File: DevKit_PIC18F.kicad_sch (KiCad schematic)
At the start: 31 parts, among them J1 PIC_ICSP_ICD, J2 USB_C_Receptacle_USB2.0_16P, J3 5P_UART, J4 RA_PORT, J5 RB_PORT, J6 RD_PORT, J7 RC_PORT, J8 RE_PORT, SW1 SW_DIP, X1 16MHz

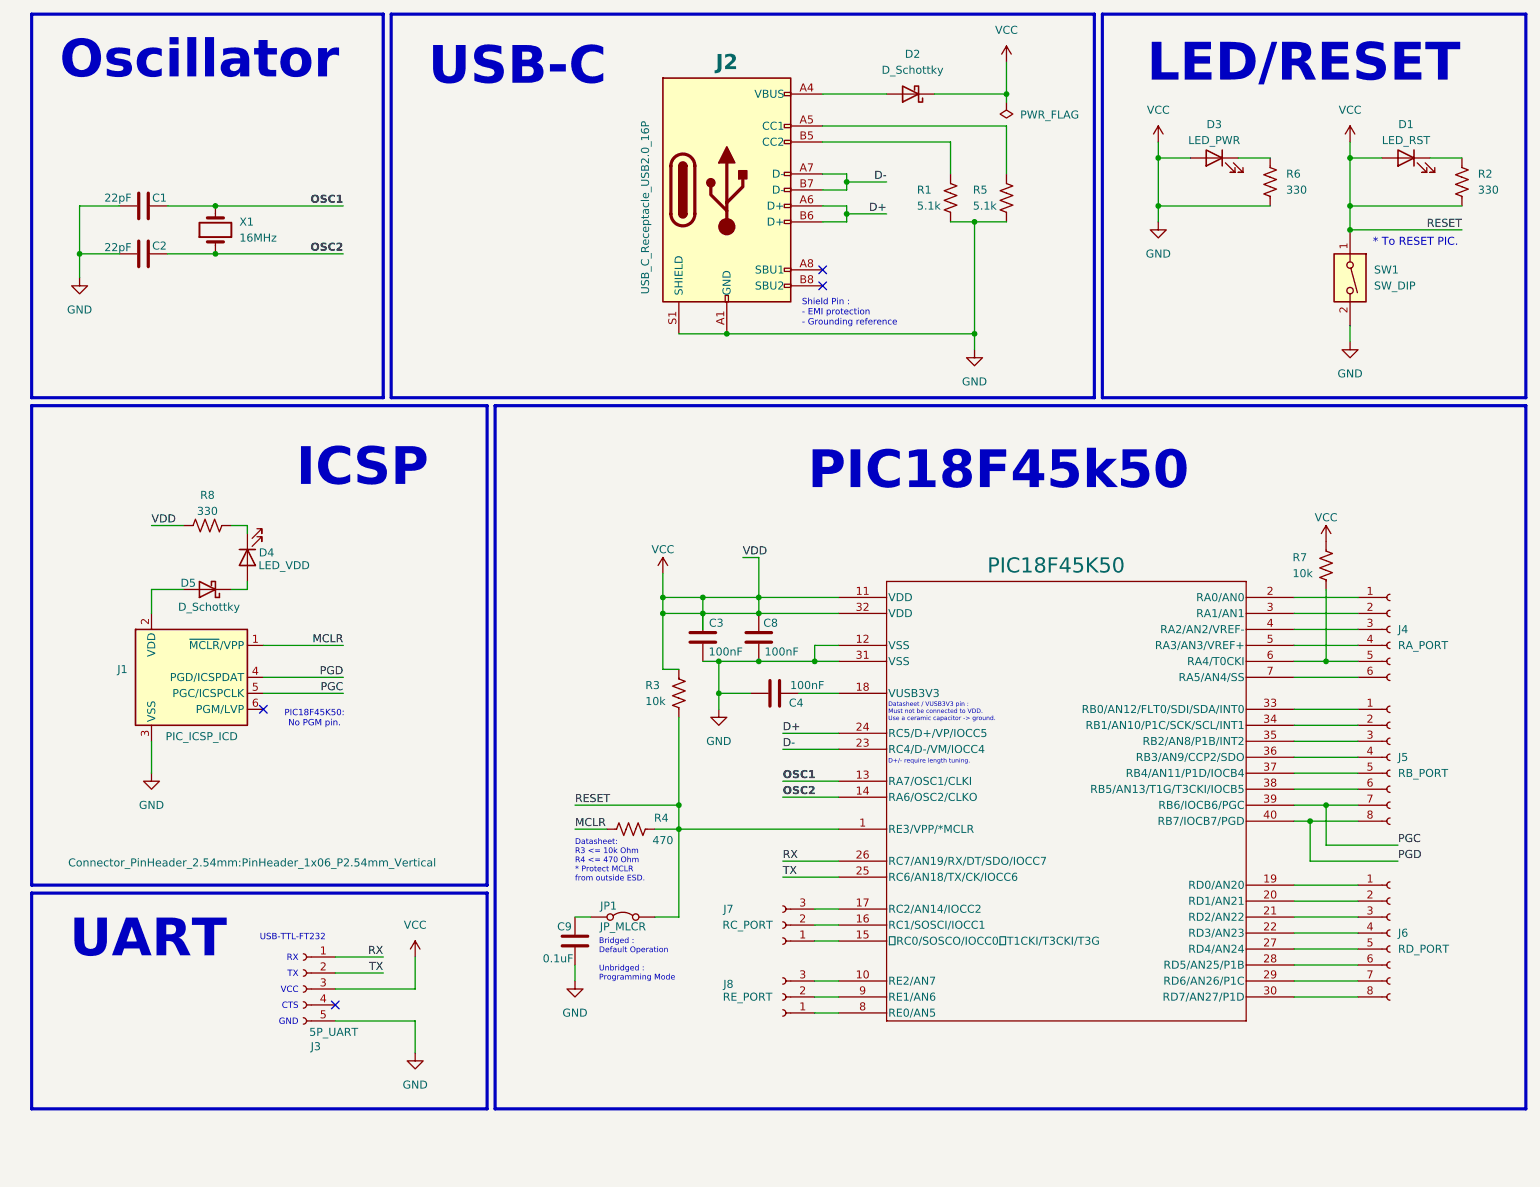
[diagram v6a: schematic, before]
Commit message: refined & ordered to fabricate test pcs.
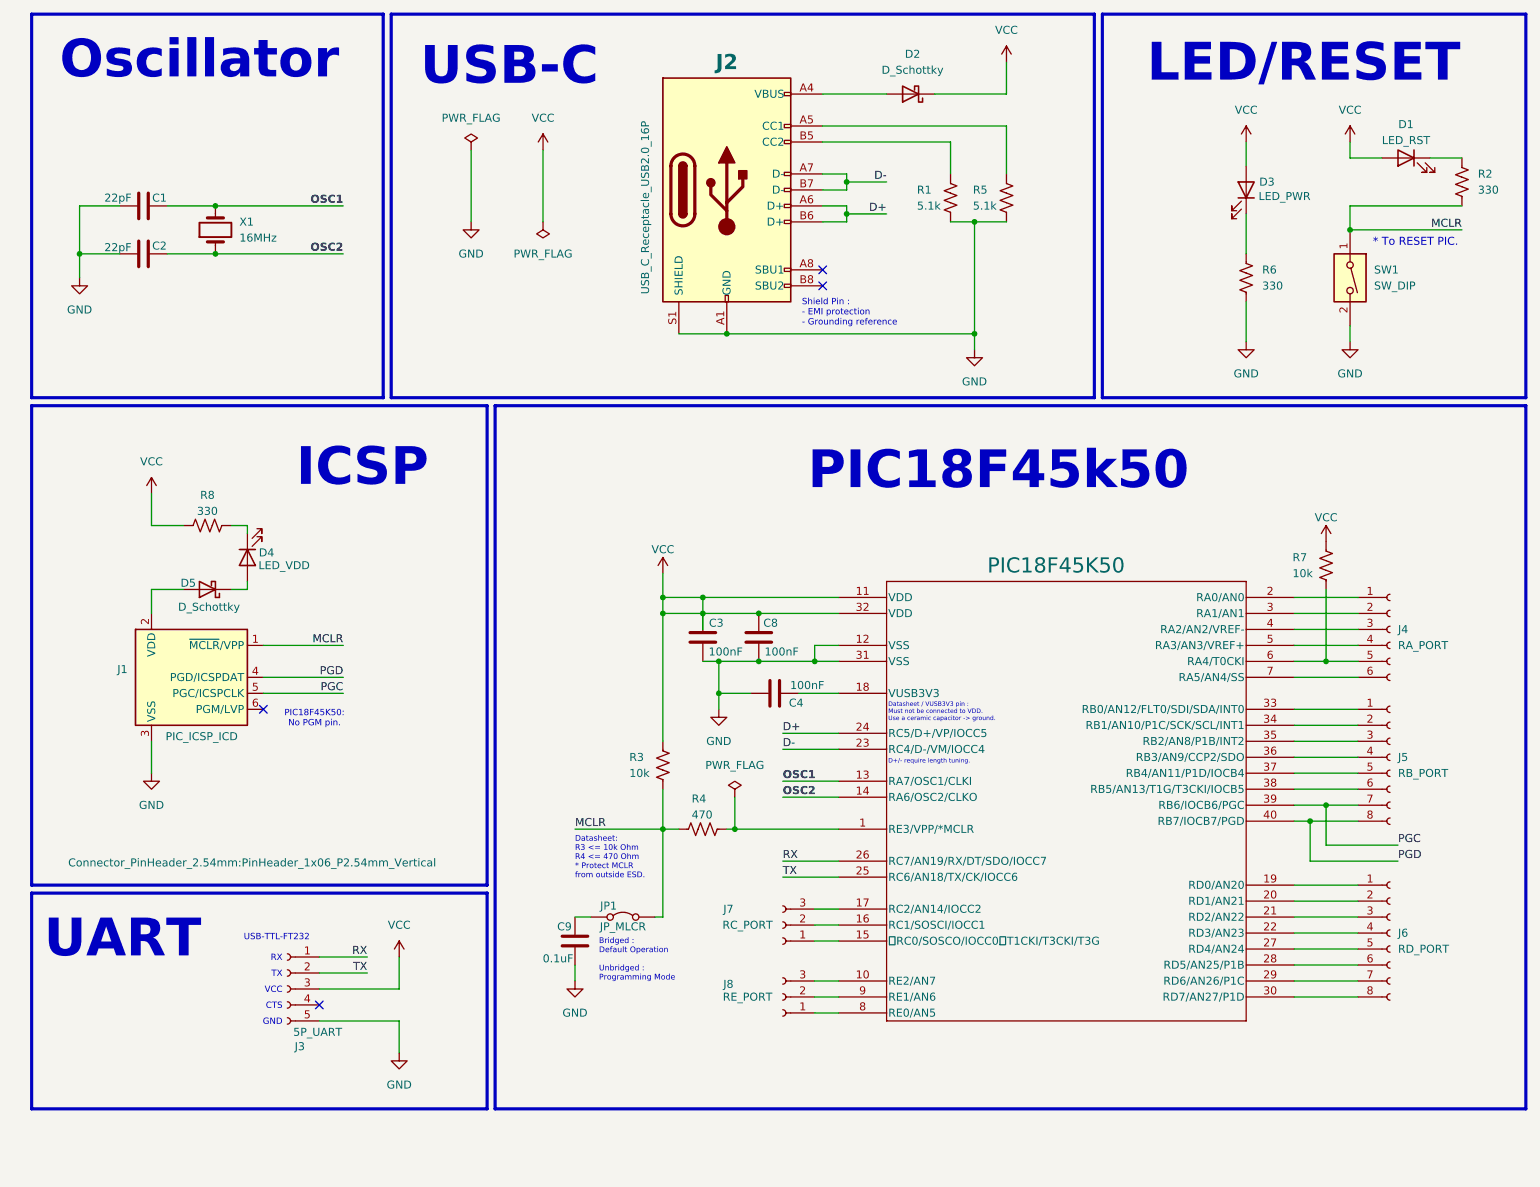
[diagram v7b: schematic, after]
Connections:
- net GND: no longer C3.1, C8.1, D1.2 (A), D2.1 (K), D3.2 (A), J3.3 (Pin_3), JP1.2 (B), PIC18F45K50.1 (RE3/VPP/*MCLR), PIC18F45K50.11 (VDD), PIC18F45K50.32 (VDD), R2.2, R3.1, R3.2, R4.2, R7.1, R8.1, SW1.1
- net MCLR: now also JP1.2 (B), R2.2, R3.2, R4.2, SW1.1; no longer R4.1
- new net: PIC18F45K50.1 (RE3/VPP/*MCLR), R4.1
- new net VCC: C3.1, C8.1, D1.2 (A), D2.1 (K), D3.2 (A), J3.3 (Pin_3), PIC18F45K50.11 (VDD), PIC18F45K50.32 (VDD), R3.1, R7.1, R8.1
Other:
- moved on the sheet: D3, J3, R3, R6

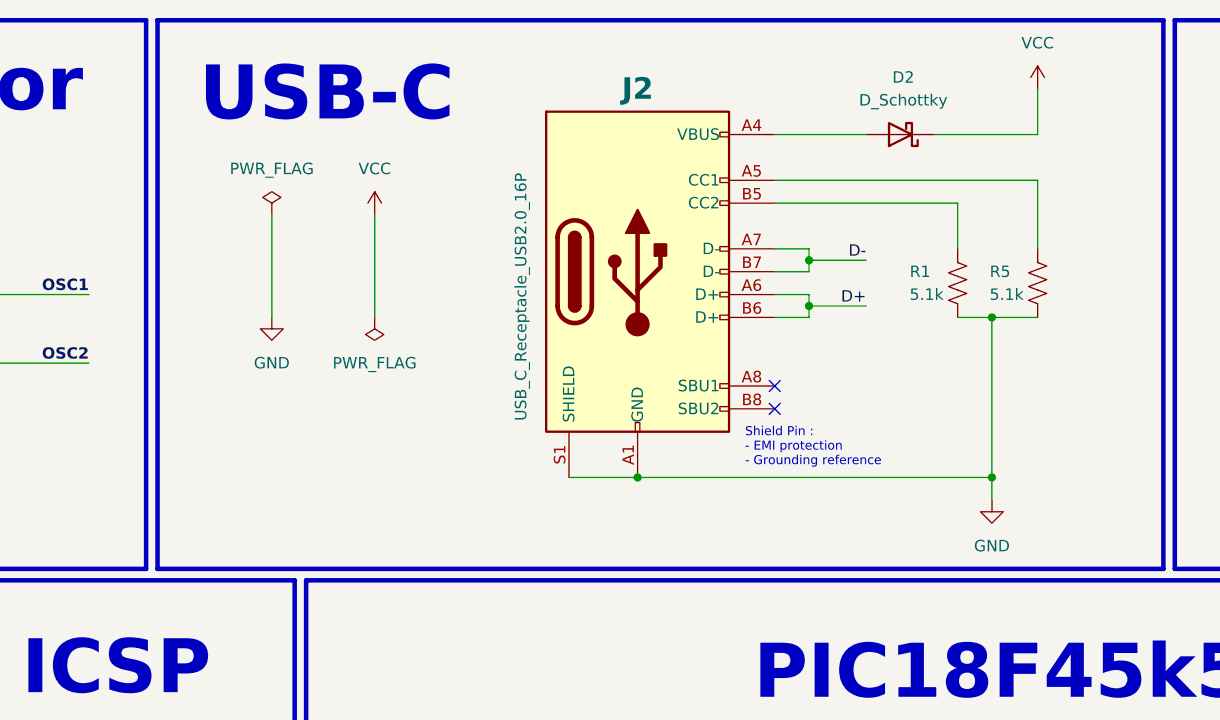
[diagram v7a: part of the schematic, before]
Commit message: Switch USB-C -> USB-B for availability.
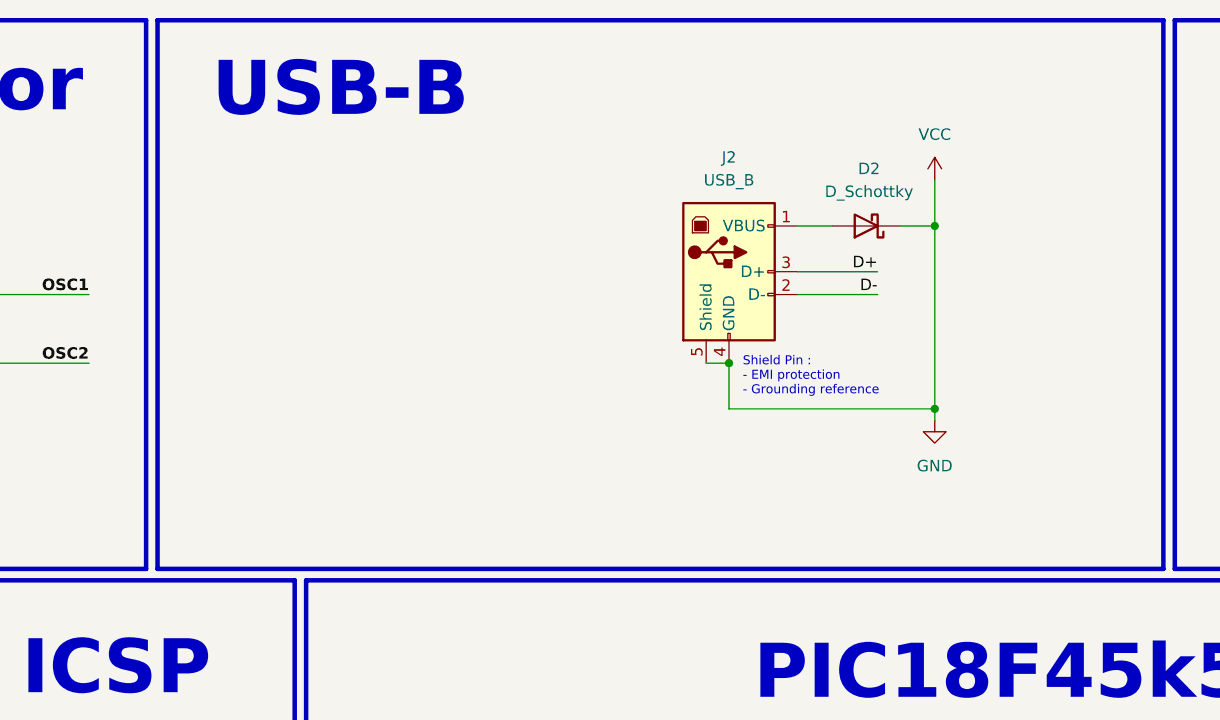
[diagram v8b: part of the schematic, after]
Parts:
- removed J2: USB_C_Receptacle_USB2.0_16P, Connector_USB:USB_C_Receptacle_GCT_USB4085, symbol Connector:USB_C_Receptacle_USB2.0_16P
- removed R1, R5: 5.1k, Resistor_THT:R_Axial_DIN0204_L3.6mm_D1.6mm_P5.08mm_Horizontal, symbol Device:R_US
- added J2: USB_B, Connector_USB:USB_B_Lumberg_2411_02_Horizontal, symbol Connector:USB_B
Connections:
- net VCC is gone; now on net GND: C3.1, C8.1, D1.2 (A), D2.1 (K), D3.2 (A), J3.3 (Pin_3), PIC18F45K50.11 (VDD), PIC18F45K50.32 (VDD), R3.1, R7.1, R8.1
- net D+: now also J2.3 (D+)
- net D-: now also J2.2 (D-)
- net GND: now also J2.4 (GND), J2.5 (Shield)
- net at D2.2 (A): now also J2.1 (VBUS)
- no-connect marks 4 -> 2
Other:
- note added: "USB-B"
- note removed: "USB-C"
- moved on the sheet: D2
